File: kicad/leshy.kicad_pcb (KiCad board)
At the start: 2 copper layers, 50 x 50 mm, 863 parts, among them J1 USER_SW, J2 SD_SW, J3 IDD, K1 SWD, K2 MICROSD_TFP09-2-12B, K3 VIN, K4 B1_18, SW1 RESET, SW2 PA0, U1 STM32F030F4P6, U2 1117-3.3, U3 MCP1700-3302

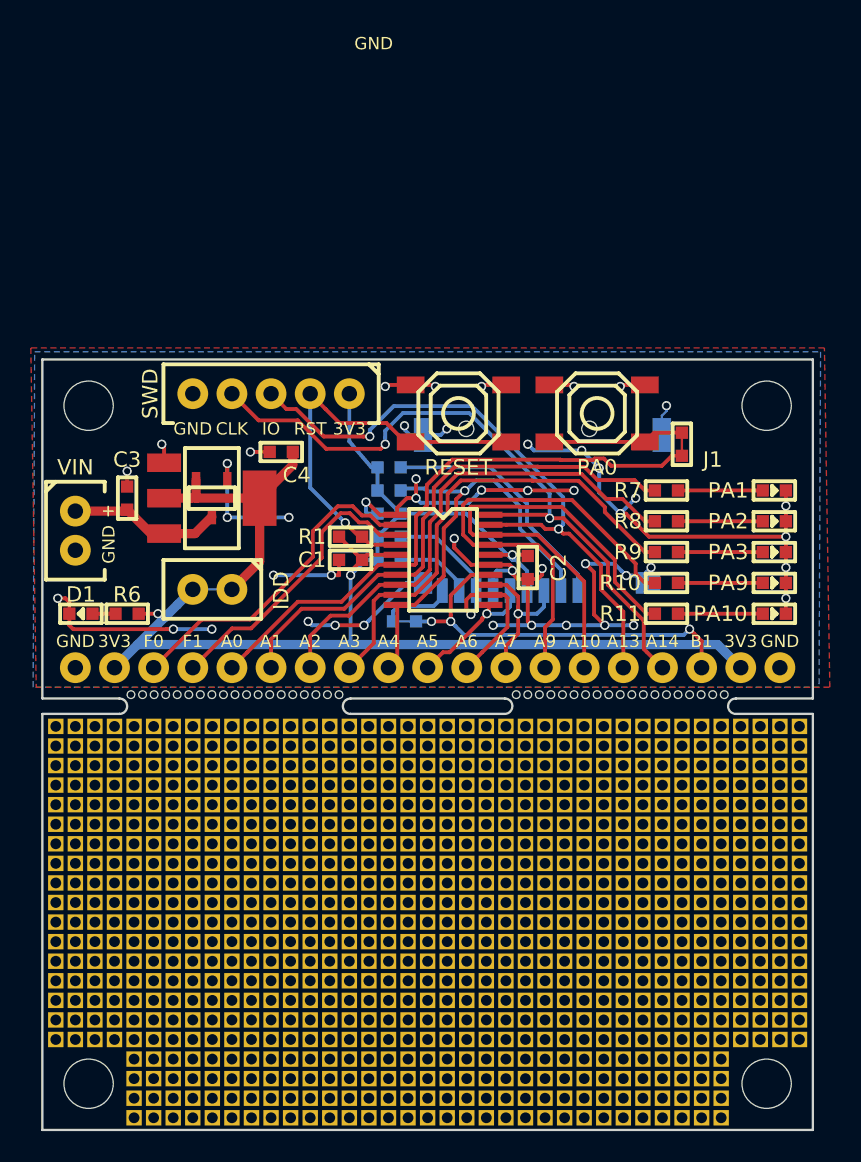
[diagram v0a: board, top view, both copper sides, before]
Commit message: Add new board revision
Main differences are:
- The SD card now has a MOSFET, so it can be completely shut off
- More (hopefully useful) silkscreen text
- Logo on board
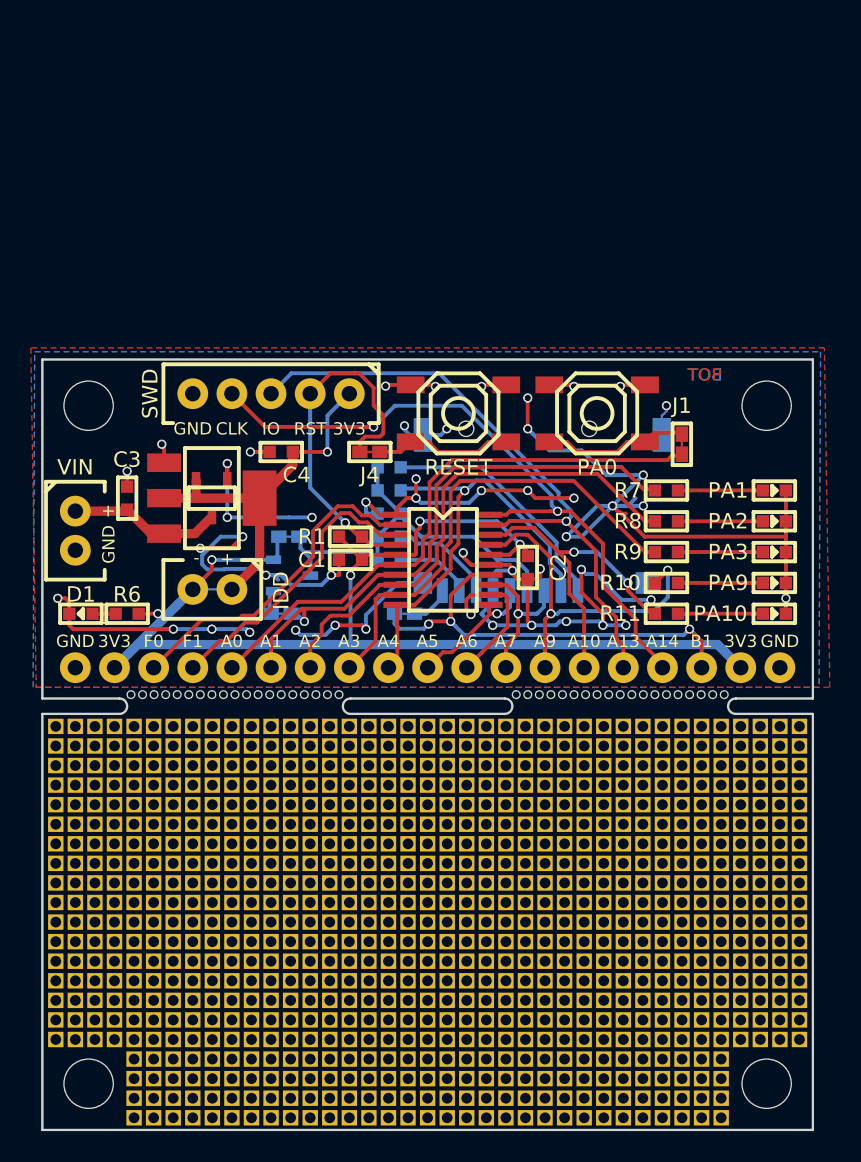
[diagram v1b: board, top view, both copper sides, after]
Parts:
- added G***: LOGO, logo:logo, B.Cu at (75.2, 43.2)
- added J4: NRST_SW, rcl:SOLDER_JUMPER_0603_B, F.Cu at (51.2, 36.0)
- added J5: SD_PWR, rcl:SOLDER_JUMPER_0603_B, B.Cu at (46.0, 41.5)
- added J6: SD_ON, rcl:SOLDER_JUMPER_0603_B, B.Cu at (45.5, 46.5)
- added Q1: IRLML6401, sot:SOT23, B.Cu at (46.2, 44.0)
- J1, J2: footprint rcl:0603_B -> rcl:SOLDER_JUMPER_0603_B
- R10, R11, R6, R7, R8, R9: value 1k -> 4k7
- moved J2 0.50 mm to (53.5, 46.5)
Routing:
- net GND: track 130.4 -> 166.6 mm
- net +3,3V: track 108.6 -> 135.7 mm, vias 3 -> 6
- net /LED5: track 31.6 -> 21.8 mm, vias 0 -> 2
- net /NRST: track 27.3 -> 35.2 mm
- net /LED4: track 30.8 -> 23.2 mm, vias 0 -> 2
- net /LED1: track 34.6 -> 39.3 mm, vias 0 -> 1
- net /PA13: track 41.4 -> 40.9 mm, vias 2 -> 1
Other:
- board text added: "-"
- board text added: "A1 ON B1 SW A4 ~CS~ A5 SCK A6 MISO A7 MOSI"
- board text added: "BOT"
- board text added: "J1: A0 (BTN) J2: B1 (SD SW) J3: IDD (3V3) J4: NRST (BTN) J5: SD PWR J6: A1 (SD ON)"
- board text added: "TOP"
- board text added: "V2.0 - 4817"
- board text added: "VIN"
